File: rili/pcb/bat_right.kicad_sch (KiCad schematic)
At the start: 21 parts, among them J11 Battery, Q1 AO3407, Q3 FS8205, SW53 SW_SPDT, U19 TP4056-42-ESOP8, U21 HT7833, U22 DW01A

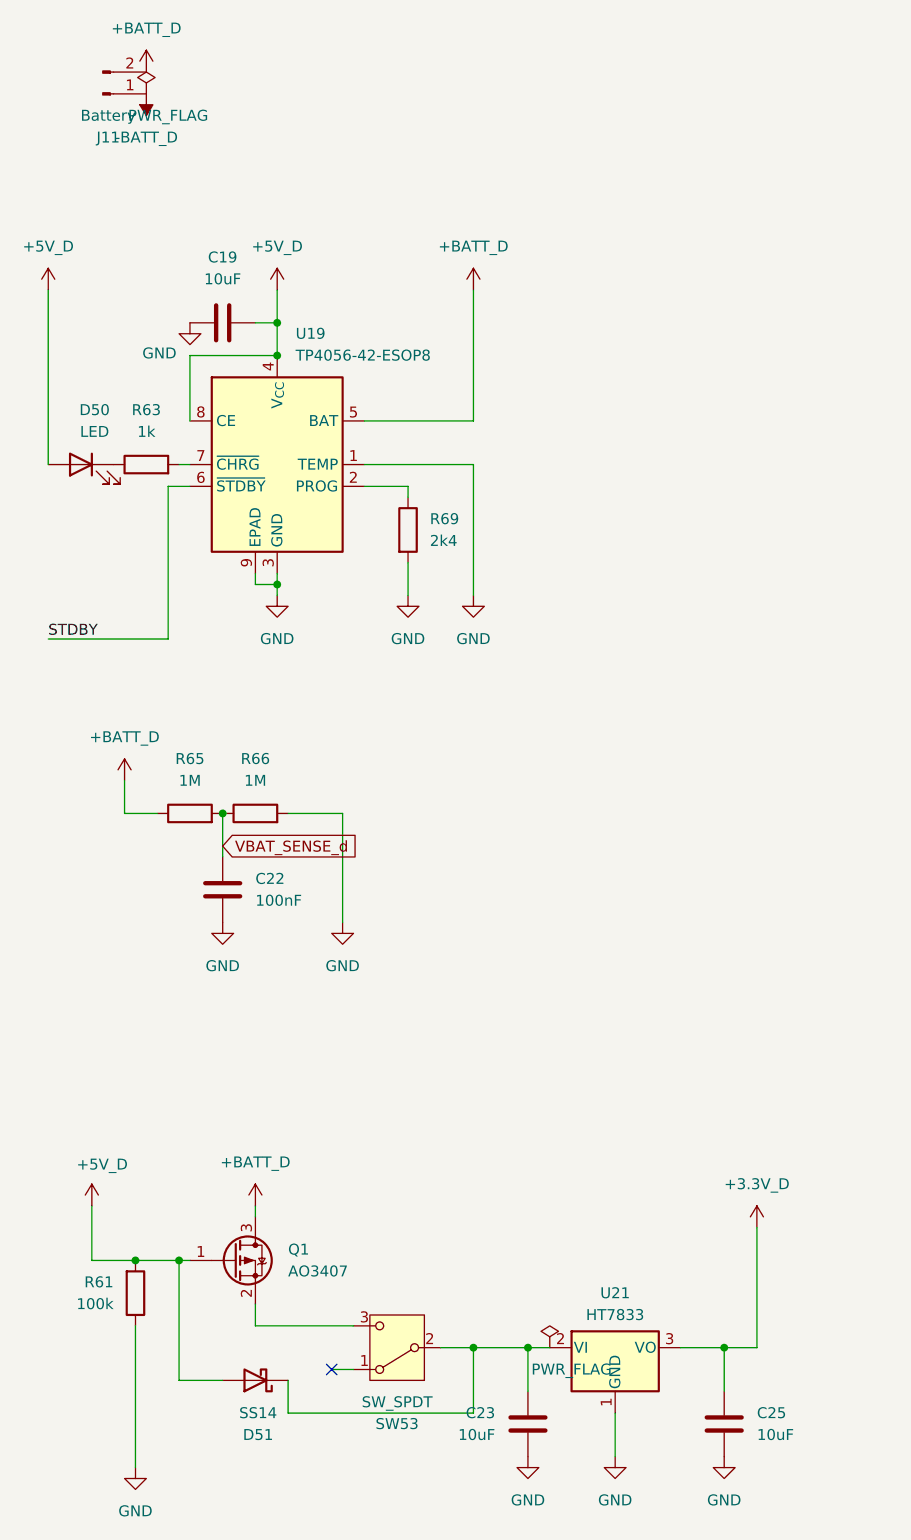
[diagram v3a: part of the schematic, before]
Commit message: review : solde complet — Tip TRRS protégé, condos +BATT, prog P4 dégagée
- TVS Tip : canal 3 des SRV05 relié au Tip des deux jacks (net TIP_5V, validé
  netlist : jack.T + load switch OUT + SRV05 sans toucher LINK_5V_EN)
- C29/C30 : 10µF sur +BATT/+BATT_D près des TP4056, placés et routés par Mae
- R48/R49 supprimés par Mae (CH334R : pull-up RESET# interne 25k, mode
  sans-quartz XO flottant conforme datasheet, fuite batterie→hub éliminée)
- pistes JP1/JP2 (prog USB du P4) écartées de la zone GND : zéro violation
- nettoyage : no_connect orpheline de la dépose R48/R49
- DRC 36/26 → 17/22 (ménage de routage par Mae), ratchet enregistré

Décisions documentées : SD manipulée hors tension (pas de TVS SD), tables de
pins matrice réelles + conventions firmware en annexe du plan v2.

Co-Authored-By: Claude Fable 5 <noreply@anthropic.com>
Claude-Session: https://claude.ai/code/session_01GfX5RmekmQi78Dm37qsT4Z
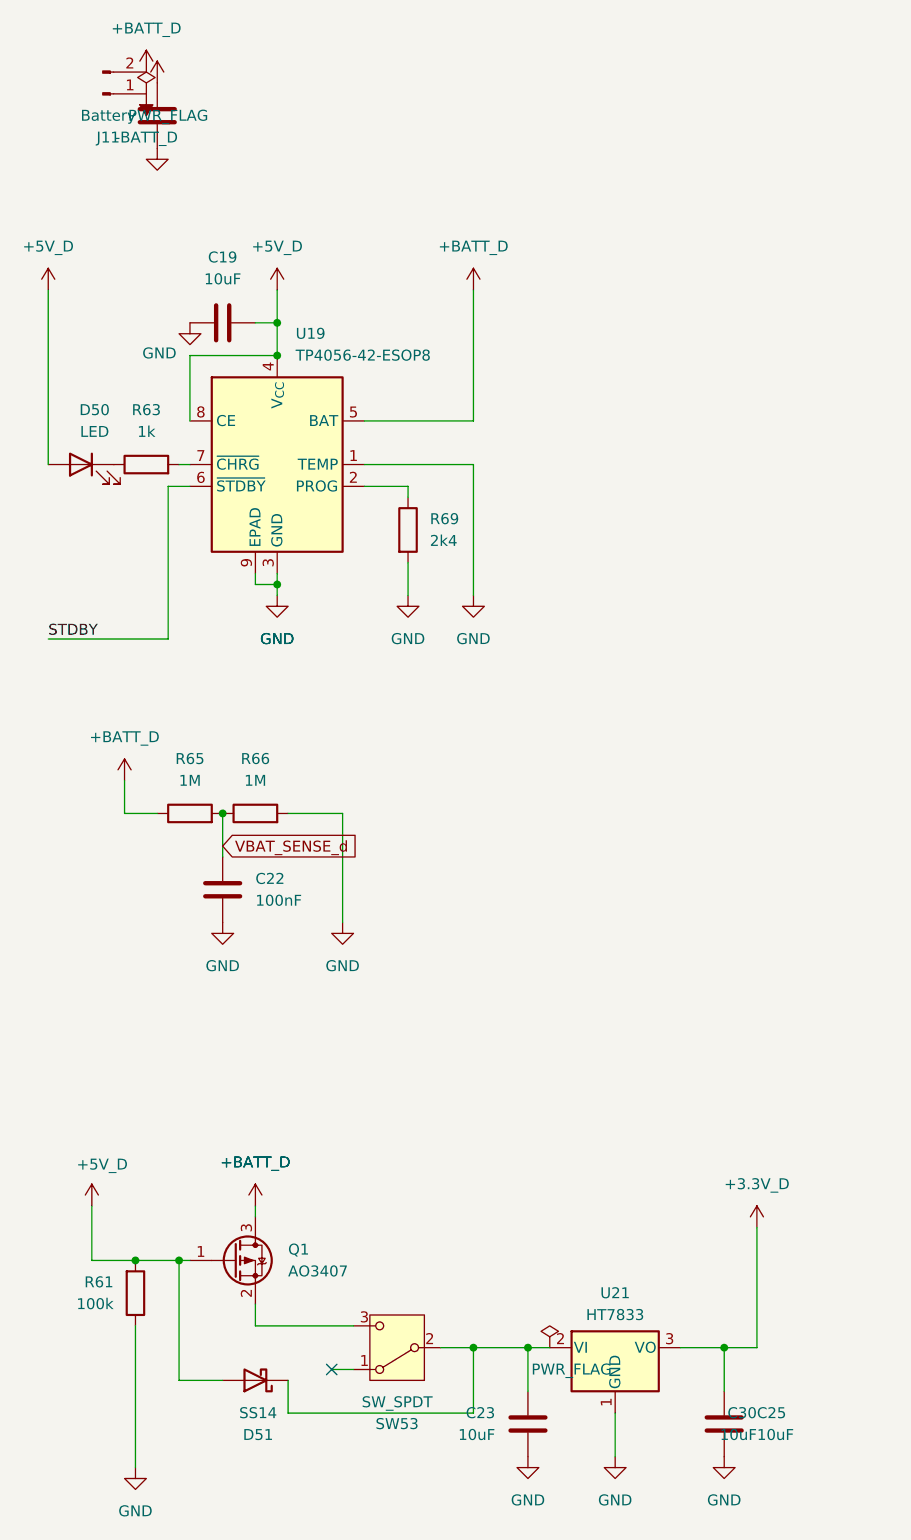
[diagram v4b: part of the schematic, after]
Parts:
- added C30: 10uF, Capacitor_SMD:C_1206_3216Metric_Pad1.33x1.80mm_HandSolder, symbol Device:C
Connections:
- net +BATT_D: now also C30.1
- net GND: now also C30.2
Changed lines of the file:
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@@
+	)
+	(symbol
+		(lib_id "power:GND")
+		(at 33.02 30.48 0)
+		(unit 1)
+		(body_style 1)
+		(exclude_from_sim no)
+		(in_bom yes)
+		(on_board yes)
+		(in_pos_files yes)
+		(dnp no)
+		(fields_autoplaced yes)
+		(property "Reference" "#PWR0925"
+			(at 46.99 88.9 0)
+			(hide yes)
+			(show_name no)
+			(do_not_autoplace no)
+			(effects
+				(font
+					(size 1.27 1.27)
+				)
+			)
+		)
+		(property "Value" "GND"
+			(at 46.99 87.63 0)
+			(show_name no)
+			(do_not_autoplace no)
+			(effects
+				(font
+					(size 1.27 1.27)
+				)
+			)
+		)
+		(property "Footprint" ""
+			(at 46.99 82.55 0)
+			(hide yes)
+			(show_name no)
+			(do_not_autoplace no)
+			(effects
+				(font
+					(size 1.27 1.27)
+				)
+			)
+		)
+		(property "Datasheet" ""
+			(at 46.99 82.55 0)
+			(hide yes)
+			(show_name no)
+			(do_not_autoplace no)
+			(effects
+				(font
+					(size 1.27 1.27)
+				)
+			)
+		)
+		(property "Description" "Power symbol creates a global label with name \"GND\" , ground"
+			(at 46.99 82.55 0)
+			(hide yes)
+			(show_name no)
+			(do_not_autoplace no)
+			(effects
+				(font
+					(size 1.27 1.27)
+				)
+			)
+		)
+		(pin "1"
+		)
+		(instances
+			(project "niphar"
+				(path "/7138aad8-3c5f-41d0-9987-adc2f08f0576/3003147c-cc6e-4474-bfa6-490b1011c122"
+					(reference "#PWR0925")
+					(unit 1)
+				)
+			)
+		)
 	)
 	(symbol
@@
 	)
 	(symbol
+		(lib_id "Device:C")
+		(at 33.02 26.67 0)
+		(unit 1)
+		(body_style 1)
+		(exclude_from_sim no)
+		(in_bom yes)
+		(on_board yes)
+		(in_pos_files yes)
+		(dnp no)
+		(fields_autoplaced yes)
+		(property "Reference" "C30"
+			(at 102.87 177.7999 0)
+			(show_name no)
+			(do_not_autoplace no)
+			(effects
+				(font
+					(size 1.27 1.27)
+				)
+				(justify right)
+			)
+		)
+		(property "Value" "10uF"
+			(at 102.87 180.3399 0)
+			(show_name no)
+			(do_not_autoplace no)
+			(effects
+				(font
+					(size 1.27 1.27)
+				)
+				(justify right)
+			)
+		)
+		(property "Footprint" "Capacitor_SMD:C_1206_3216Metric_Pad1.33x1.80mm_HandSolder"
+			(at 98.0948 175.26 0)
+			(hide yes)
+			(show_name no)
+			(do_not_autoplace no)
+			(effects
+				(font
+					(size 1.27 1.27)
+				)
+			)
+		)
+		(property "Datasheet" ""
+			(at 99.06 179.07 0)
+			(hide yes)
+			(show_name no)
+			(do_not_autoplace no)
+			(effects
+				(font
+					(size 1.27 1.27)
+				)
+			)
+		)
+		(property "Description" "Unpolarized capacitor"
+			(at 99.06 179.07 0)
+			(hide yes)
+			(show_name no)
+			(do_not_autoplace no)
+			(effects
+				(font
+					(size 1.27 1.27)
+				)
+			)
+		)
+		(pin "2"
+		)
+		(pin "1"
+		)
+		(instances
+			(project "niphar"
+				(path "/7138aad8-3c5f-41d0-9987-adc2f08f0576/3003147c-cc6e-4474-bfa6-490b1011c122"
+					(reference "C30")
+					(unit 1)
+				)
+			)
+		)
+	)
+	(symbol
 		(lib_id "Diode:SS14")
 		(at 44.45 173.99 180)
@@
 					(unit 1)
 				)
+			)
+		)
+	)
+	(symbol
+		(lib_id "power:+BATT")
+		(at 33.02 22.86 0)
+		(unit 1)
+		(body_style 1)
+		(exclude_from_sim no)
+		(in_bom yes)
+		(on_board yes)
+		(in_pos_files yes)
+		(dnp no)
+		(fields_autoplaced yes)
+		(property "Reference" "#PWR0924"
+			(at 44.45 157.48 0)
+			(hide yes)
+			(show_name no)
+			(do_not_autoplace no)
+			(effects
+				(font
+					(size 1.27 1.27)
+				)
+			)
+		)
+		(property "Value" "+BATT_D"
+			(at 44.45 148.59 0)
+			(show_name no)
+			(do_not_autoplace no)
+			(effects
+				(font
+					(size 1.27 1.27)
+				)
+			)
+		)
+		(property "Footprint" ""
+			(at 44.45 153.67 0)
+			(hide yes)
+			(show_name no)
+			(do_not_autoplace no)
+			(effects
+				(font
+					(size 1.27 1.27)
+				)
+			)
+		)
+		(property "Datasheet" ""
+			(at 44.45 153.67 0)
+			(hide yes)
+			(show_name no)
+			(do_not_autoplace no)
+			(effects
+				(font
+					(size 1.27 1.27)
+				)
+			)
+		)
+		(property "Description" "Power symbol creates a global label with name \"+BATT\""
+			(at 44.45 153.67 0)
+			(hide yes)
+			(show_name no)
+			(do_not_autoplace no)
+			(effects
+				(font
+					(size 1.27 1.27)
+				)
+			)
+		)
+		(pin "1"
+		)
+		(instances
+			(project "niphar"
+				(path "/7138aad8-3c5f-41d0-9987-adc2f08f0576/3003147c-cc6e-4474-bfa6-490b1011c122"
+					(reference "#PWR0924")
+					(unit 1)
+				)
